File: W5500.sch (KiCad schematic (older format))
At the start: 29 parts, among them J5 RJ45_Amphenol_RJMG1BD3B8K1ANR, U6 W5500, Y2 25MHz

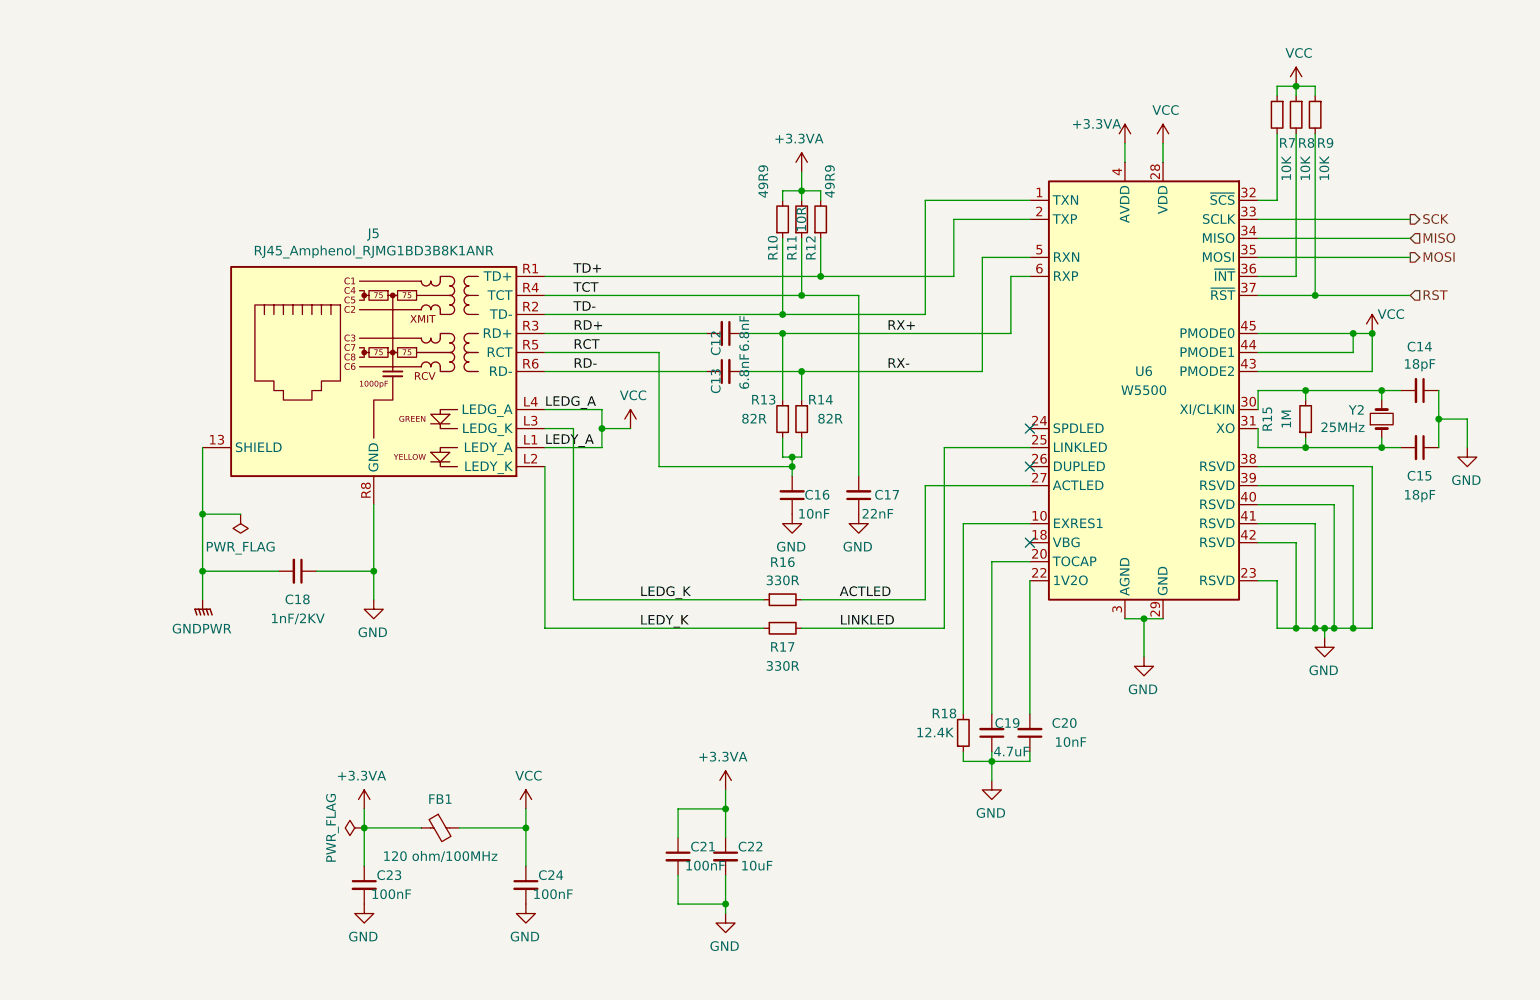
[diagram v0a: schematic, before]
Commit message: W5500 fixes
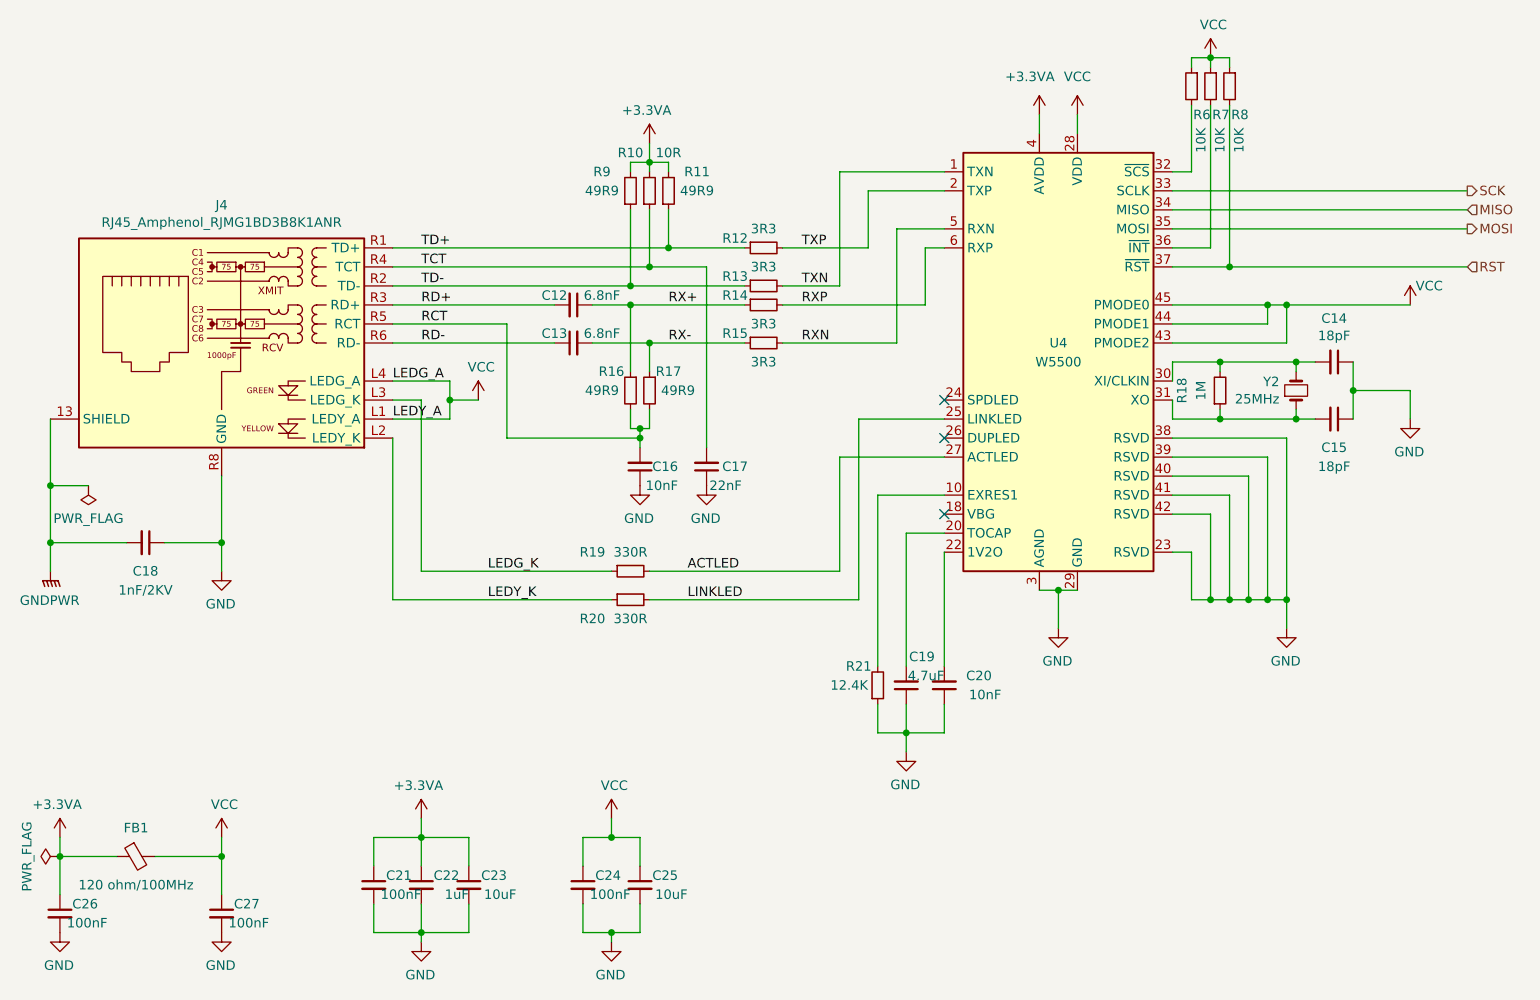
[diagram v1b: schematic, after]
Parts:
- added C22: 1uF, Capacitor_SMD:C_0603_1608Metric, symbol Device:C_Small
- added C24: 100nF, Capacitor_SMD:C_0603_1608Metric, symbol Device:C_Small
- added C25: 10uF, Capacitor_SMD:C_0603_1608Metric, symbol Device:C_Small
- added R12, R13, R14, R15: 3R3, Resistor_SMD:R_0603_1608Metric, symbol Device:R_Small
- R16: renamed from R13; value 82R -> 49R9
- R17: renamed from R14; value 82R -> 49R9
- renumbered C22 to C23, C23 to C26, C24 to C27, J5 to J4, R11 to R10, R12 to R11, R15 to R18, R16 to R19, R17 to R20, R18 to R21, R7 to R6, R8 to R7, R9 to R8, R10 to R9, U6 to U4
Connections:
- net +3.3VA: now also C22.1
- net GND: now also C22.2, C24.2, C25.2
- net RX+: now also R14.1; no longer U4.6 (RXP)
- net RX-: now also R15.1; no longer U4.5 (RXN)
- net TD+: now also R12.1; no longer U4.2 (TXP)
- net TD-: now also R13.1; no longer U4.1 (TXN)
- net VCC: now also C24.1, C25.1
- new net RXN: R15.2, U4.5 (RXN)
- new net RXP: R14.2, U4.6 (RXP)
- new net TXN: R13.2, U4.1 (TXN)
- new net TXP: R12.2, U4.2 (TXP)
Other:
- moved on the sheet: C12, C13, C14, C15, C16, C17, C18, C19, C20, C21, C23, C26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

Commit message: cleanup
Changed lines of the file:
@@
 AR Path="/61BA974E" Ref="R?"  Part="1"
 AR Path="/61B89C6B/61BA974E" Ref="R19"  Part="1"
-F 0 "R19" V 5000 4250 50  0000 C CNN
-F 1 "330R" V 5000 4050 50  0000 C CNN
+F 0 "R19" V 4950 4250 50  0000 C CNN
+F 1 "330R" V 5050 4250 50  0000 C CNN
 F 2 "Resistor_SMD:R_0603_1608Metric" H 5100 4050 50  0001 C CNN
 F 3 "~" H 5100 4050 50  0001 C CNN
@@
 AR Path="/61B89C6B/61BA9754" Ref="R20"  Part="1"
 F 0 "R20" V 5200 4400 50  0000 C CNN
-F 1 "330R" V 5200 4200 50  0000 C CNN
+F 1 "330R" V 5300 4400 50  0000 C CNN
 F 2 "Resistor_SMD:R_0603_1608Metric" H 5100 4200 50  0001 C CNN
 F 3 "~" H 5100 4200 50  0001 C CNN
@@
 AR Path="/61A135B1" Ref="R?"  Part="1"
 AR Path="/61B89C6B/61A135B1" Ref="R12"  Part="1"
-F 0 "R12" V 5750 2500 50  0000 C CNN
-F 1 "3R3" V 5700 2350 50  0000 C CNN
+F 0 "R12" V 5650 2500 50  0000 C CNN
+F 1 "3R3" V 5750 2500 50  0000 C CNN
 F 2 "Resistor_SMD:R_0603_1608Metric" H 5800 2350 50  0001 C CNN
 F 3 "~" H 5800 2350 50  0001 C CNN
@@
 AR Path="/61B89C6B/61A14842" Ref="R14"  Part="1"
 F 0 "R14" V 5750 2800 50  0000 C CNN
-F 1 "3R3" V 5900 2650 50  0000 C CNN
+F 1 "3R3" V 5850 2800 50  0000 C CNN
 F 2 "Resistor_SMD:R_0603_1608Metric" H 5800 2650 50  0001 C CNN
 F 3 "~" H 5800 2650 50  0001 C CNN
@@
 AR Path="/61B89C6B/61A150A0" Ref="R15"  Part="1"
 F 0 "R15" V 5750 3000 50  0000 C CNN
-F 1 "3R3" V 5900 2850 50  0000 C CNN
+F 1 "3R3" V 5850 3000 50  0000 C CNN
 F 2 "Resistor_SMD:R_0603_1608Metric" H 5800 2850 50  0001 C CNN
 F 3 "~" H 5800 2850 50  0001 C CNN
@@
 AR Path="/61A156E9" Ref="R?"  Part="1"
 AR Path="/61B89C6B/61A156E9" Ref="R13"  Part="1"
-F 0 "R13" V 5750 2700 50  0000 C CNN
-F 1 "3R3" V 5700 2550 50  0000 C CNN
+F 0 "R13" V 5650 2700 50  0000 C CNN
+F 1 "3R3" V 5750 2700 50  0000 C CNN
 F 2 "Resistor_SMD:R_0603_1608Metric" H 5800 2550 50  0001 C CNN
 F 3 "~" H 5800 2550 50  0001 C CNN

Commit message: final version
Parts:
- renumbered C12 to C11, C13 to C12, C14 to C13, C15 to C14, C16 to C15, C17 to C16, C18 to C17, C19 to C18, C20 to C19, C21 to C20, C22 to C21, C23 to C22, C24 to C23, C25 to C24, C26 to C25, C27 to C26

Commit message: buck converter
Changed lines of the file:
@@
 Sheet 2 2
 Title "Celestron Ethernet Adapter"
-Date "2021-11-17"
-Rev "1.0"
+Date "2021-11-25"
+Rev "1.1"
 Comp "Hyiger Designs"
 Comment1 ""
@@
 P 2100 5550
 AR Path="/61BA9817" Ref="#FLG?"  Part="1"
-AR Path="/61B89C6B/61BA9817" Ref="#FLG04"  Part="1"
-F 0 "#FLG04" H 2100 5625 50  0001 C CNN
+AR Path="/61B89C6B/61BA9817" Ref="#FLG03"  Part="1"
+F 0 "#FLG03" H 2100 5625 50  0001 C CNN
 F 1 "PWR_FLAG" H 2100 5723 50  0000 C CNN
 F 2 "" H 2100 5550 50  0001 C CNN
@@
 P 2250 3600
 AR Path="/61BA981D" Ref="#FLG?"  Part="1"
-AR Path="/61B89C6B/61BA981D" Ref="#FLG03"  Part="1"
-F 0 "#FLG03" H 2250 3675 50  0001 C CNN
+AR Path="/61B89C6B/61BA981D" Ref="#FLG02"  Part="1"
+F 0 "#FLG02" H 2250 3675 50  0001 C CNN
 F 1 "PWR_FLAG" H 2250 3773 50  0000 C CNN
 F 2 "" H 2250 3600 50  0001 C CNN
@@
 Wire Wire Line
 	8250 2450 9500 2450
+$Comp
+L power:PWR_FLAG #FLG?
+U 1 1 61B23586
+P 2950 5550
+AR Path="/61B23586" Ref="#FLG?"  Part="1"
+AR Path="/61B89C6B/61B23586" Ref="#FLG0101"  Part="1"
+F 0 "#FLG0101" H 2950 5625 50  0001 C CNN
+F 1 "PWR_FLAG" H 2950 5723 50  0000 C CNN
+F 2 "" H 2950 5550 50  0001 C CNN
+F 3 "~" H 2950 5550 50  0001 C CNN
+	1    2950 5550
+	0    1    1    0
+$EndComp
+$Comp
+L power:PWR_FLAG #FLG?
+U 1 1 61B348A3
+P 4850 5950
+AR Path="/61B348A3" Ref="#FLG?"  Part="1"
+AR Path="/61B89C6B/61B348A3" Ref="#FLG0102"  Part="1"
+F 0 "#FLG0102" H 4850 6025 50  0001 C CNN
+F 1 "PWR_FLAG" H 4850 6123 50  0000 C CNN
+F 2 "" H 4850 5950 50  0001 C CNN
+F 3 "~" H 4850 5950 50  0001 C CNN
+	1    4850 5950
+	0    -1   -1   0
+$EndComp
 $EndSCHEMATC
